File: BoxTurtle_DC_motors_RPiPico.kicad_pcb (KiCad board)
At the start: 4 copper layers, 99.1 x 73.7 mm, 80 parts, among them J1 Power input, J10 DC motor 1, J11 DC motor 2, J12 DC motor 3, J13 DC motor 4, J14 Screw_Terminal_01x02, J15 CAN, J2 Power input, J3 Power output, J4 Power output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

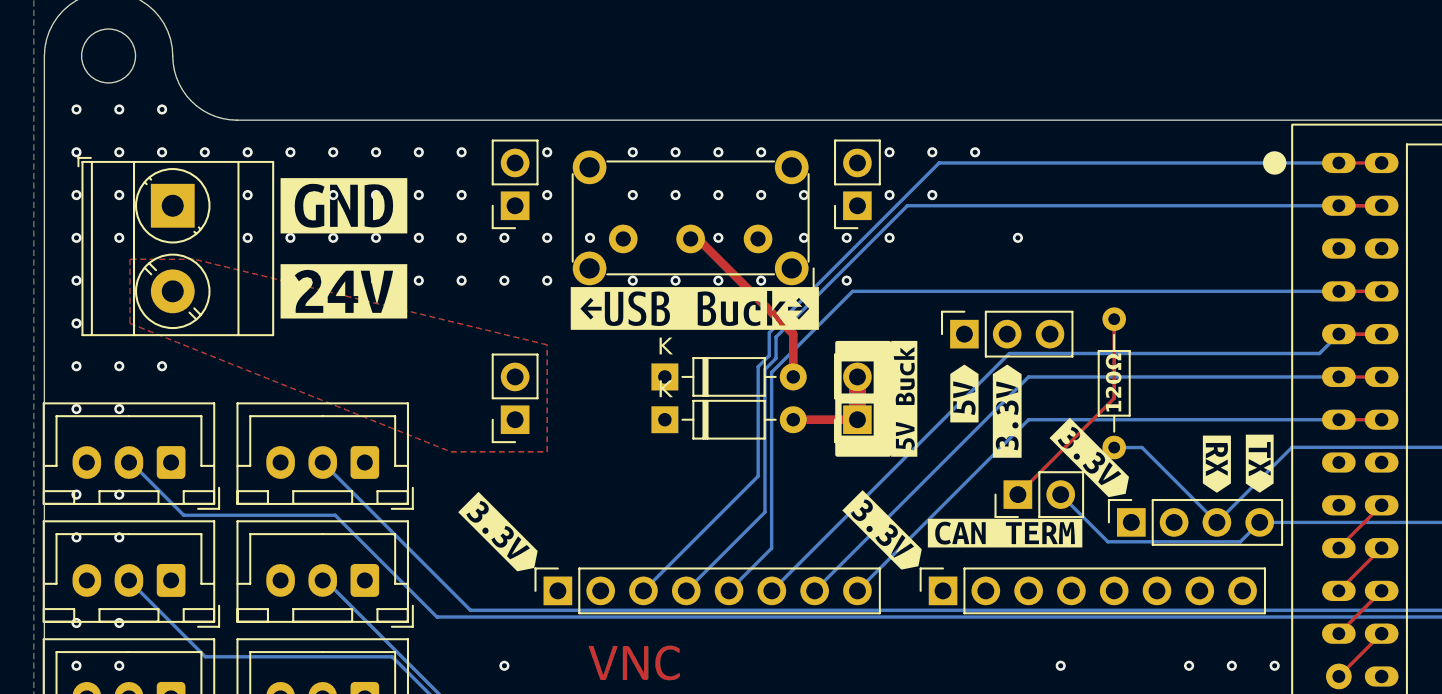
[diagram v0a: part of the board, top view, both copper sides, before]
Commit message: Fuse & Gerber
Added the fuse for safety, also uploaded Gerber files for those who want to make their own board.
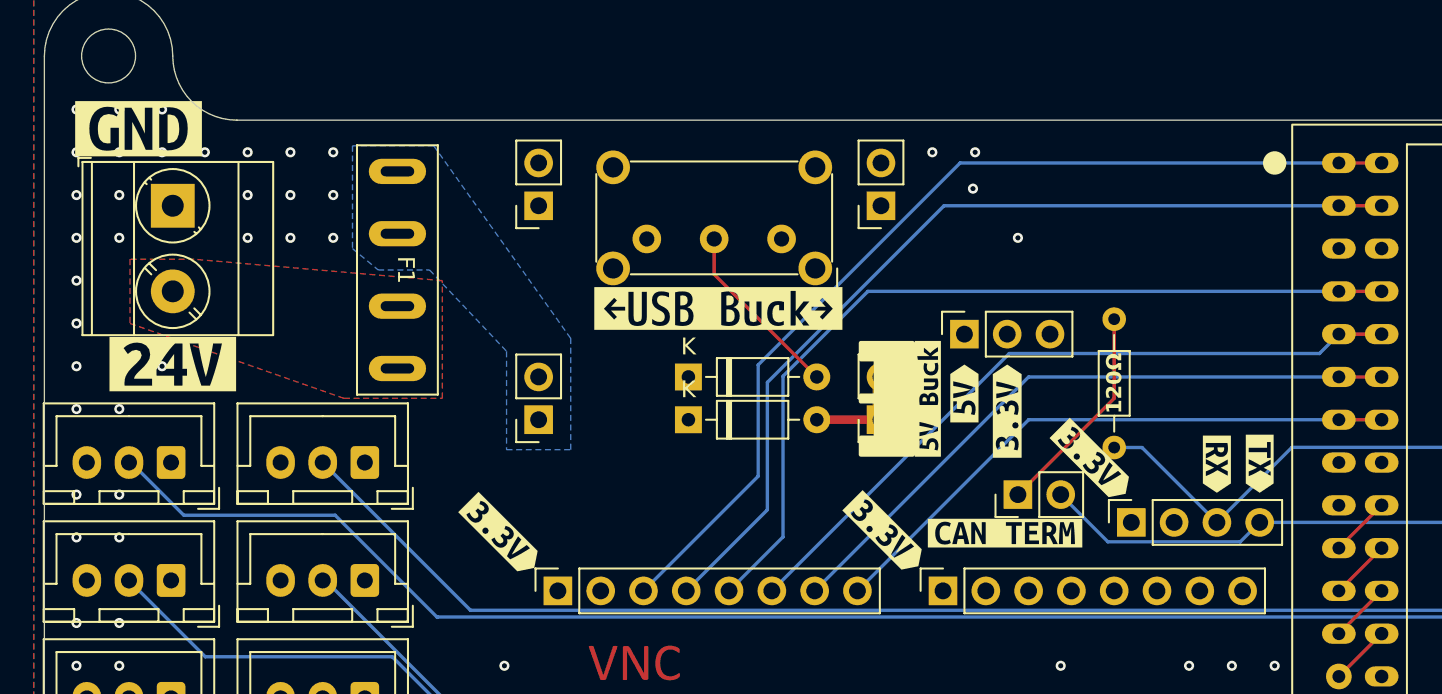
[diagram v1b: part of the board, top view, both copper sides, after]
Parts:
- added F1: Fuse_Small, XF-506P:XF-506P, F.Cu at (114.9, 52.1)
- SW13: value SW_SPDT -> EG1224
- U2: value ~ -> Black Pill STM32F401
- moved kibuzzard-679EE0D3 13.0 mm to (99.6, 43.7)
- moved kibuzzard-679EE0F2 11.0 mm to (101.6, 57.7)
- moved kibuzzard-67A00B69 1.40 mm to (134.0, 54.4)
- moved kibuzzard-67A00BD4 1.40 mm to (134.0, 54.4)
- moved D1 1.40 mm to (132.2, 58.4)
- moved D2 1.40 mm to (132.2, 61.0)
- moved J1 1.40 mm to (123.3, 61.0)
- moved J2 1.40 mm to (123.3, 48.3)
- moved J3 1.40 mm to (143.6, 61.0)
- moved J4 1.40 mm to (143.6, 48.3)
- moved SW13 1.40 mm to (137.7, 50.2)
- moved kibuzzard-67A0CA07 1.40 mm to (146.4, 59.7)
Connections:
- J14 pad 2: VCC -> VCCQ
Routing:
- net DC1_1: track 56.4 -> 55.2 mm
- net VBUS: track 117.9 -> 116.6 mm
- net SLP_1: track 58.9 -> 58.2 mm
- net DC2_1: track 52.2 -> 51.7 mm
- net GND: vias 152 -> 113
- added copper zone on B.Cu, net VCC
- added copper zone on F.Cu, net VCCQ
- removed copper zone on F.Cu, net VCC
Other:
- board text added: "BoxTurtle DC motors standalone board Rev 2.2"
- board text removed: "BoxTurtle DC motors standalone board Rev 2.1"
